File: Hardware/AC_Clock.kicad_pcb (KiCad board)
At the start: 2 copper layers, 101.6 x 175.3 mm, 63 parts, among them J1 L, J2 N, J3 Conn_01x10, J4 Conn_01x10, J5 Minutes, J6 Hours, J7 PWR, J8 PWR, Q1 BSS138, SW3 Hour Set, SW4 Min Set, T1 F12-500-C2, U1 AZ1117-5.0, U10 4511, U11 HDSP-816E, U13 HDSP-816E, U15 4510, U16 4027, U17 4081, U2 LTV-817S, U3 4040, U4 4518, U6 4511, U7 HDSP-816E, U8 4511, U9 HDSP-816E

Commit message: chore: Update to KiCAD 9.0
Clear out old pcb design to start fresh.

Signed-off-by: Joel Cranmer <42.joel.cranmer@gmail.com>
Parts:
- removed C1: 10u, Capacitor_SMD:C_0603_1608Metric
- removed C10: Safety, Capacitor_THT:C_Disc_D10.5mm_W5.0mm_P7.50mm
- removed C2: 22u, Capacitor_SMD:C_0603_1608Metric
- removed C3, C6, C7, C8: 0.1u, Capacitor_SMD:C_0603_1608Metric
- removed D1: ABS2, Diode_SMD:Diode_Bridge_Diotec_ABS
- removed D2, D3, D4, D5: 1N4148WT, Diode_SMD:D_SOD-523
- removed D20: PM, LED_THT:LED_D5.0mm
- removed F1: LVR005NS, Fuse:Fuse_BelFuse_0ZRE0005FF_L8.3mm_W3.8mm
- removed J1: L, JKC_Library:Keystone_1287
- removed J2: N, JKC_Library:Keystone_1287
- removed J3, J4: Conn_01x10, Connector_PinSocket_2.54mm:PinSocket_1x10_P2.54mm_Vertical
- removed J5: Minutes, Connector_PinHeader_2.54mm:PinHeader_1x10_P2.54mm_Horizontal
- removed J6: Hours, Connector_PinHeader_2.54mm:PinHeader_1x10_P2.54mm_Horizontal
- removed J7: PWR, Connector_PinSocket_2.54mm:PinSocket_1x03_P2.54mm_Vertical
- removed J8: PWR, Connector_PinHeader_2.54mm:PinHeader_1x03_P2.54mm_Vertical
- removed Q1: BSS138, Package_TO_SOT_SMD:SOT-363_SC-70-6
- removed R1, R2, R3: 1k, Resistor_SMD:R_0603_1608Metric
- removed REF** (x10): MountingHole_3.2mm_M3, MountingHole:MountingHole_3.2mm_M3
- removed REF** (x2): LED_D5.0mm, LED_THT:LED_D5.0mm
- removed RN1, RN2, RN3, RN4, RN5, RN6, RN7: 1k, Resistor_SMD:R_Array_Convex_4x0603
- removed RV1: V180ZA, Varistor:RV_Disc_D7mm_W5.1mm_P5mm
- removed SW3: Hour Set, JKC_Library:SW_Push_CK_PN11SBNA03QE_SPDT_Right_Angle
- removed SW4: Min Set, JKC_Library:SW_Push_CK_PN11SBNA03QE_SPDT_Right_Angle
- removed T1: F12-500-C2, JKC_Library:XFMR_Triad_F12-500-C2
- removed U1: AZ1117-5.0, Package_TO_SOT_SMD:SOT-223-3_TabPin2
- removed U10, U6, U8: 4511, Package_SO:TSSOP-16_4.4x5mm_P0.65mm
- removed U11, U13, U7, U9: HDSP-816E, JKC_Library:Broadcom_HDSP-81x
- removed U15: 4510, Package_DIP:DIP-16_W7.62mm
- removed U16: 4027, Package_DIP:DIP-16_W7.62mm
- removed U17: 4081, Package_DIP:DIP-14_W7.62mm
- removed U2: LTV-817S, Package_DIP:SMDIP-4_W9.53mm
- removed U3: 4040, Package_DIP:DIP-16_W7.62mm
- removed U4: 4518, Package_DIP:DIP-16_W7.62mm
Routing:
- net +5V: track 374.5 -> 0.00 mm, vias 4 -> 0
- net /2Hz: track 104.2 -> 0.00 mm
- net /minute: track 92.3 -> 0.00 mm
- net /min: track 70.6 -> 0.00 mm
- net DB_3: track 60.5 -> 0.00 mm
- net DA_3: track 58.0 -> 0.00 mm, vias 2 -> 0
- net Net-(U16B-C): track 57.4 -> 0.00 mm
- net GND: track 57.0 -> 0.00 mm, vias 18 -> 0
- net /10Hr: track 56.9 -> 0.00 mm
- net Net-(U15-PE): track 55.4 -> 0.00 mm, vias 2 -> 0
- net /hour: track 55.2 -> 0.00 mm, vias 2 -> 0
- net DD_1: track 51.3 -> 0.00 mm
- net DB_2: track 50.2 -> 0.00 mm
- net DC_2: track 49.3 -> 0.00 mm, vias 1 -> 0
- net Earth: track 47.1 -> 0.00 mm
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- removed copper zone on B.Cu, net Earth
- removed copper zone on B.Cu, net GND
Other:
- board outline removed

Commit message: feat: Create new PCB layout (draft)
Signed-off-by: Joel Cranmer <42.joel.cranmer@gmail.com>
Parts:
- added C1: 0.33u, Capacitor_SMD:C_0603_1608Metric, F.Cu at (86.4, 125.7)
- added C2: 0.1u, Capacitor_SMD:C_0603_1608Metric, F.Cu at (86.4, 123.2)
- added C3: 0.1u, Capacitor_SMD:C_0603_1608Metric, F.Cu at (73.7, 106.7)
- added D1: RS203, Diode_THT:Diode_Bridge_Vishay_KBPM, F.Cu at (115.7, 125.7)
- added D2: 1N4148WT, Diode_SMD:D_SOD-523, F.Cu at (86.4, 130.8)
- added D3: Col1, LED_THT:LED_D5.0mm, F.Cu at (109.2, 53.3)
- added D4: Col2, LED_THT:LED_D5.0mm, F.Cu at (108.0, 61.0)
- added D5: PM, LED_THT:LED_D5.0mm, F.Cu at (77.5, 52.1)
- added F1: 500mA, JKC_Library:Fuse_Schurter_MST_250, F.Cu at (81.3, 149.9)
- added HS1: Heatsink, JKC_Library:Heatsink_TO220_CUI_HSS-B20-NP-02, F.Cu at (74.1, 124.5)
- added J1: L, JKC_Library:Keystone_1287, F.Cu at (81.3, 165.1)
- added J3: N, JKC_Library:Keystone_1287, F.Cu at (135.9, 165.1)
- added Q1: 2N3906, Package_TO_SOT_THT:TO-92_Inline_Wide, F.Cu at (110.5, 73.7)
- added Q2: 2N3904, Package_TO_SOT_THT:TO-92_Inline_Wide, F.Cu at (77.5, 73.7)
- added R1: 2k1, Resistor_SMD:R_0603_1608Metric, F.Cu at (86.4, 128.3)
- added R2: 1k, Resistor_SMD:R_0603_1608Metric, F.Cu at (86.4, 120.7)
- added R3: 1k, Resistor_SMD:R_0603_1608Metric, F.Cu at (105.4, 71.1)
- added R4: 1k, Resistor_SMD:R_0603_1608Metric, F.Cu at (82.5, 68.6)
- added R5: 1k, Resistor_SMD:R_0603_1608Metric, F.Cu at (82.5, 73.7)
- added RV1: V180ZA, JKC_Library:Varistor_12mm_P7.5mm, F.Cu at (135.9, 151.2)
- added SW1: Min Set, JKC_Library:SW_Push_CK_PN11SBNA03QE_SPDT_Right_Angle, F.Cu at (135.9, 119.4)
- added SW2: Hour Set, JKC_Library:SW_Push_CK_PN11SBNA03QE_SPDT_Right_Angle, F.Cu at (135.9, 127.0)
- added T1: F12-500-C2, JKC_Library:XFMR_Triad_F12-500-C2, F.Cu at (109.2, 154.7)
- added U1: LM7805, Package_TO_SOT_THT:TO-220-3_Vertical, F.Cu at (77.5, 127.0)
- added U10: 5082-7300, JKC_Library:Display_HP_5082-7300, F.Cu at (115.6, 64.8)
- added U11: 5082-7300, JKC_Library:Display_HP_5082-7300, F.Cu at (96.5, 64.8)
- added U12: 5082-7300, JKC_Library:Display_HP_5082-7300, F.Cu at (85.1, 64.8)
- added U2: 817C, Package_DIP:DIP-4_W7.62mm_LongPads, F.Cu at (94.0, 128.3)
- added U3: 4518, Package_DIP:DIP-16_W7.62mm_Socket_LongPads, F.Cu at (123.2, 110.5)
- added U4: 4027, Package_DIP:DIP-16_W7.62mm_Socket_LongPads, F.Cu at (77.5, 88.9)
- added U5: 4081, Package_DIP:DIP-14_W7.62mm_Socket_LongPads, F.Cu at (101.6, 88.9)
- added U6: 4040, Package_DIP:DIP-16_W7.62mm_Socket_LongPads, F.Cu at (77.5, 110.5)
- added U7: 4510, Package_DIP:DIP-16_W7.62mm_Socket_LongPads, F.Cu at (123.2, 88.9)
- added U8: 4082, Package_DIP:DIP-14_W7.62mm_Socket_LongPads, F.Cu at (101.6, 110.5)
- added U9: 5082-7300, JKC_Library:Display_HP_5082-7300, F.Cu at (127.0, 64.8)
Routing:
- net +5V: track 0.00 -> 348.6 mm, vias 0 -> 5
- net /2Hz: track 0.00 -> 109.2 mm, vias 0 -> 1
- net /10Hour: track 0.00 -> 82.8 mm
- net /01_Minute/IN_{1}: track 0.00 -> 81.1 mm
- net /minute: track 0.00 -> 78.6 mm, vias 0 -> 2
- net /01_Hour/IN_{1}: track 0.00 -> 75.9 mm
- net /01_Hour/IN_{2}: track 0.00 -> 72.1 mm, vias 0 -> 1
- net /10hr: track 0.00 -> 66.3 mm
- net /10m: track 0.00 -> 65.8 mm
- net /10_Minute/IN_{1}: track 0.00 -> 65.5 mm, vias 0 -> 1
- net /hour: track 0.00 -> 63.0 mm, vias 0 -> 1
- net /01_Minute/IN_{2}: track 0.00 -> 61.8 mm
- net /10_Minute/IN_{2}: track 0.00 -> 61.1 mm, vias 0 -> 1
- net Net-(U4B-C): track 0.00 -> 60.1 mm
- net /10_Minute/IN_{4}: track 0.00 -> 59.4 mm, vias 0 -> 1
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- added copper zone on B.Cu, net /Fused
- added copper zone on B.Cu, net GND
- added copper zone on B.Cu, net Net-(T1-Pad6)
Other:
- board outline added: 73.7 x 129.5 mm

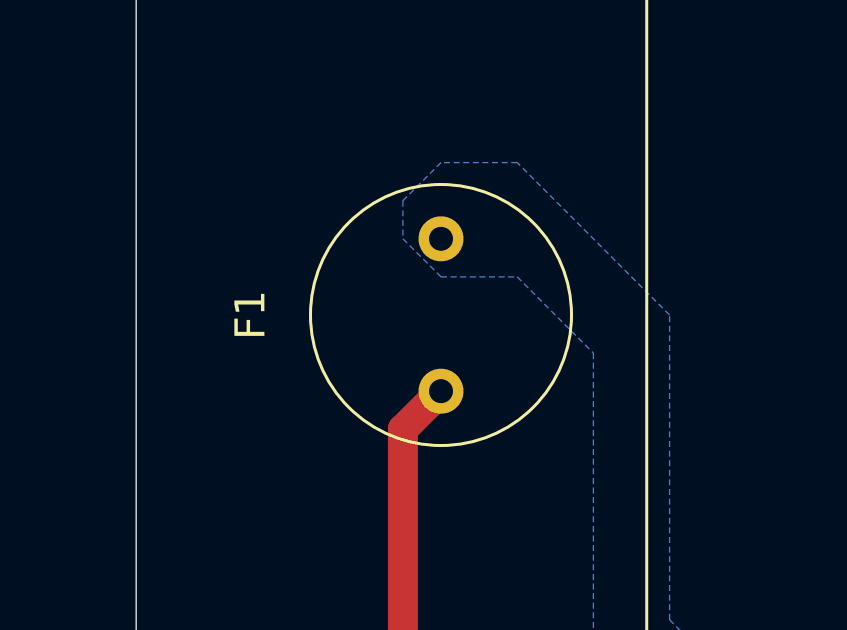
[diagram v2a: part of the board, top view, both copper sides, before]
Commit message: fix: remove unused connectors and set MPN for HS1
- Remove unused J2 J4 power connectors
- Set part number for heatsink

Signed-off-by: Joel Cranmer <42.joel.cranmer@gmail.com>
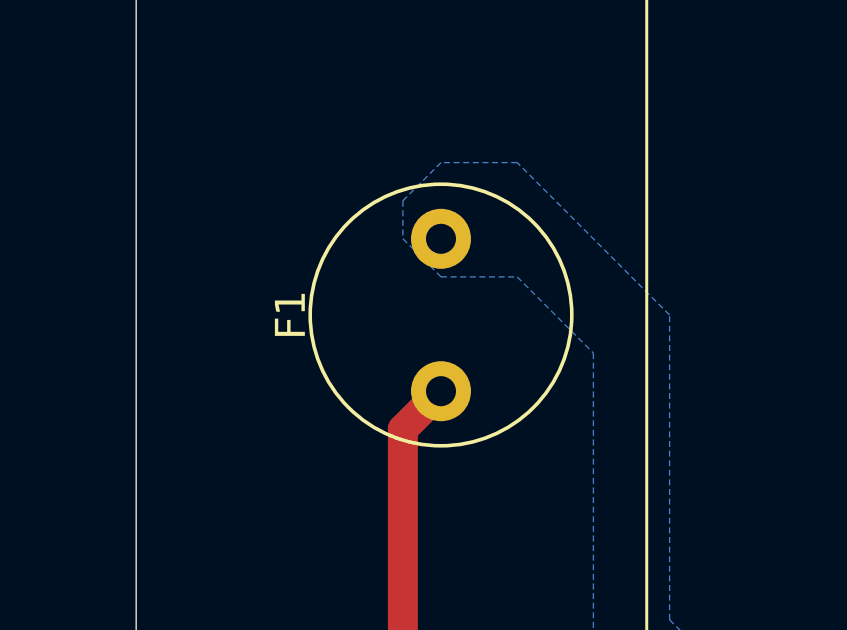
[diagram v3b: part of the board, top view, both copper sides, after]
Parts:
- F1: footprint JKC_Library:Fuse_Schurter_MST_250 -> Fuse:Fuse_Littelfuse_372_D8.50mm
- moved F1 2.54 mm to (81.3, 152.4)
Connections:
- U3 pad 2: /min -> unconnected-(U3A-Enable-Pad2)
- U3 pad 3: /01_Minute/IN_{1} -> /01_Minute/IN_{4}
- U3 pad 5: /01_Minute/IN_{4} -> /01_Minute/IN_{1}
- U3 pad 6: /10m -> unconnected-(U3A-Q4-Pad6)
- U3 pad 7: GND -> unconnected-(U3A-Reset-Pad7)
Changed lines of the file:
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@@
 	(net 59 "unconnected-(U11-DP-Pad4)")
 	(net 60 "unconnected-(U12-DP-Pad4)")
+	(net 61 "unconnected-(U3A-Enable-Pad2)")
+	(net 62 "unconnected-(U3A-Q4-Pad6)")
+	(net 63 "unconnected-(U3A-Reset-Pad7)")
 	(footprint "Diode_SMD:D_SOD-523"
 		(layer "F.Cu")
@@
 		)
 	)
-	(footprint "JKC_Library:Fuse_Schurter_MST_250"
+	(footprint "Fuse:Fuse_Littelfuse_372_D8.50mm"
 		(layer "F.Cu")
-		(at 81.28 149.86 90)
+		(at 81.28 152.4 90)
+		(descr "Fuse, Littelfuse, 372, 8.5x8mm, https://www.littelfuse.com/~/media/electronics/datasheets/fuses/littelfuse_fuse_372_datasheet.pdf.pdf")
+		(tags "fuse tht radial")
 		(property "Reference" "F1"
-			(at 0 -6.35 90)
-			(unlocked yes)
+			(at 2.54 -5 90)
 			(layer "F.SilkS")
 			(effects
 				(font
 					(size 1 1)
-					(thickness 0.1)
+					(thickness 0.15)
 				)
 			)
 		)
 		(property "Value" "500mA"
-			(at 0 1 90)
-			(unlocked yes)
+			(at 2.54 5 90)
 			(layer "F.Fab")
 			(effects
@@
 			(effects
 				(font
-					(size 1 1)
+					(size 1.27 1.27)
 					(thickness 0.15)
 				)
@@
 			(effects
 				(font
-					(size 1 1)
+					(size 1.27 1.27)
 					(thickness 0.15)
 				)
 			)
 		)
-		(property "MPN" "0034.6612"
+		(property "MPN" "MRT 500-BULK"
 			(at 0 0 90)
 			(unlocked yes)
@@
 		(attr through_hole)
 		(fp_circle
-			(center 0 0)
-			(end 4.35 0)
+			(center 2.54 0)
+			(end 6.9 0)
 			(stroke
-				(width 0.1)
-				(type default)
+				(width 0.12)
+				(type solid)
 			)
 			(fill no)
@@
 		)
 		(fp_circle
-			(center 0 0)
-			(end 4.75 0)
+			(center 2.54 0)
+			(end 7.04 0)
 			(stroke
-				(width 0.1)
+				(width 0.05)
 				(type solid)
 			)
@@
 		)
 		(fp_circle
-			(center 0 0)
-			(end 4.25 0)
+			(center 2.54 0)
+			(end 6.79 0)
 			(stroke
 				(width 0.1)
-				(type default)
+				(type solid)
 			)
 			(fill no)
@@
 		)
 		(fp_text user "${REFERENCE}"
-			(at 0 2.5 90)
-			(unlocked yes)
+			(at 2.54 0 90)
 			(layer "F.Fab")
 			(effects
@@
 		)
 		(pad "1" thru_hole circle
-			(at -2.54 0 90)
-			(size 1.5 1.5)
-			(drill 0.8)
+			(at 0 0 90)
+			(size 2 2)
+			(drill 1)
 			(layers "*.Cu" "*.Mask")
 			(remove_unused_layers no)
@@
 		)
 		(pad "2" thru_hole circle
-			(at 2.54 0 90)
-			(size 1.5 1.5)
-			(drill 0.8)
+			(at 5.08 0 90)
+			(size 2 2)
+			(drill 1)
 			(layers "*.Cu" "*.Mask")
 			(remove_unused_layers no)
@@
 		)
 		(embedded_fonts no)
+		(model "${KICAD9_3DMODEL_DIR}/Fuse.3dshapes/Fuse_Littelfuse_372_D8.50mm.step"
+			(offset
+				(xyz 0 0 0)
+			)
+			(scale
+				(xyz 1 1 1)
+			)
+			(rotate
+				(xyz 0 0 0)
+			)
+		)
 	)
 	(footprint "Package_DIP:DIP-16_W7.62mm_Socket_LongPads"
@@
 			(layers "*.Cu" "*.Mask")
 			(remove_unused_layers no)
-			(net 19 "/min")
+			(net 61 "unconnected-(U3A-Enable-Pad2)")
 			(pinfunction "Enable")
 			(pintype "input")
@@
 			(layers "*.Cu" "*.Mask")
 			(remove_unused_layers no)
-			(net 28 "/01_Minute/IN_{1}")
+			(net 29 "/01_Minute/IN_{4}")
 			(pinfunction "Q1")
 			(pintype "output")
@@
 			(layers "*.Cu" "*.Mask")
 			(remove_unused_layers no)
-			(net 29 "/01_Minute/IN_{4}")
+			(net 28 "/01_Minute/IN_{1}")
 			(pinfunction "Q3")
 			(pintype "output")
@@
 			(layers "*.Cu" "*.Mask")
 			(remove_unused_layers no)
-			(net 27 "/10m")
+			(net 62 "unconnected-(U3A-Q4-Pad6)")
 			(pinfunction "Q4")
 			(pintype "output")
@@
 			(layers "*.Cu" "*.Mask")
 			(remove_unused_layers no)
-			(net 1 "GND")
+			(net 63 "unconnected-(U3A-Reset-Pad7)")
 			(pinfunction "Reset")
 			(pintype "input")

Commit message: fix: U3A flipped
Somehow the U3 package was mirrored unexpectedly. Fixed back to
the correct orientation

Signed-off-by: Joel Cranmer <42.joel.cranmer@gmail.com>
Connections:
- U3 pad 2: unconnected-(U3A-Enable-Pad2) -> /min
- U3 pad 3: /01_Minute/IN_{4} -> /01_Minute/IN_{1}
- U3 pad 5: /01_Minute/IN_{1} -> /01_Minute/IN_{4}
- U3 pad 6: unconnected-(U3A-Q4-Pad6) -> /10m
- U3 pad 7: unconnected-(U3A-Reset-Pad7) -> GND
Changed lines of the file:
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@@
 	(net 59 "unconnected-(U11-DP-Pad4)")
 	(net 60 "unconnected-(U12-DP-Pad4)")
-	(net 61 "unconnected-(U3A-Enable-Pad2)")
-	(net 62 "unconnected-(U3A-Q4-Pad6)")
-	(net 63 "unconnected-(U3A-Reset-Pad7)")
 	(footprint "Diode_SMD:D_SOD-523"
 		(layer "F.Cu")
@@
 			)
 		)
+		(property "MPN" "HSS-B20-NP-02"
+			(at 0 0 270)
+			(unlocked yes)
+			(layer "F.Fab")
+			(hide yes)
+			(effects
+				(font
+					(size 1 1)
+					(thickness 0.15)
+				)
+			)
+		)
 		(property ki_fp_filters "Heatsink_*")
 		(sheetname "/")
@@
 			(layers "*.Cu" "*.Mask")
 			(remove_unused_layers no)
-			(net 61 "unconnected-(U3A-Enable-Pad2)")
+			(net 19 "/min")
 			(pinfunction "Enable")
 			(pintype "input")
@@
 			(layers "*.Cu" "*.Mask")
 			(remove_unused_layers no)
-			(net 29 "/01_Minute/IN_{4}")
+			(net 28 "/01_Minute/IN_{1}")
 			(pinfunction "Q1")
 			(pintype "output")
@@
 			(layers "*.Cu" "*.Mask")
 			(remove_unused_layers no)
-			(net 28 "/01_Minute/IN_{1}")
+			(net 29 "/01_Minute/IN_{4}")
 			(pinfunction "Q3")
 			(pintype "output")
@@
 			(layers "*.Cu" "*.Mask")
 			(remove_unused_layers no)
-			(net 62 "unconnected-(U3A-Q4-Pad6)")
+			(net 27 "/10m")
 			(pinfunction "Q4")
 			(pintype "output")
@@
 			(layers "*.Cu" "*.Mask")
 			(remove_unused_layers no)
-			(net 63 "unconnected-(U3A-Reset-Pad7)")
+			(net 1 "GND")
 			(pinfunction "Reset")
 			(pintype "input")
